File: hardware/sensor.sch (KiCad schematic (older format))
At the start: 4 parts

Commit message: Finished Modulator; still needs Values doe; Fixed Symbol for the HC4046
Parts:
- added C1, C2: C_Small, symbol C_Small
- added R1, R2, R3, R?: R_Small, symbol R_Small
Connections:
- net labels added: +3V3, GND, TX_in, TX_out
- wire segments 0 -> 13
- no-connect marks 0 -> 6
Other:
- moved on the sheet: U?
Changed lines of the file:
@@
 L CD74HC4046 U?
 U 1 1 56DDA4FD
-P 3750 2650
-F 0 "U?" H 3450 3250 60  0000 C CNN
-F 1 "CD74HC4046" H 3700 1850 60  0000 C CNN
-F 2 "Housings_SSOP:TSSOP-16_4.4x5mm_Pitch0.65mm" H 4550 1650 60  0001 C CNN
-F 3 "http://www.ti.com/lit/ds/symlink/cd74hc4046a.pdf" H 4600 1750 60  0001 C CNN
-	1    3750 2650
+P 2700 6150
+F 0 "U?" H 2400 6850 60  0000 C CNN
+F 1 "CD74HC4046" H 2650 5250 60  0000 C CNN
+F 2 "Housings_SSOP:TSSOP-16_4.4x5mm_Pitch0.65mm" H 3500 5150 60  0001 C CNN
+F 3 "http://www.ti.com/lit/ds/symlink/cd74hc4046a.pdf" H 3550 5250 60  0001 C CNN
+	1    2700 6150
 	1    0    0    -1
 $EndComp
@@
 L CD74HC4046 U?
 U 1 1 56DDA564
-P 2300 2700
-F 0 "U?" H 2000 3300 60  0000 C CNN
-F 1 "CD74HC4046" H 2250 1900 60  0000 C CNN
-F 2 "Housings_SSOP:TSSOP-16_4.4x5mm_Pitch0.65mm" H 3100 1700 60  0001 C CNN
-F 3 "http://www.ti.com/lit/ds/symlink/cd74hc4046a.pdf" H 3150 1800 60  0001 C CNN
-	1    2300 2700
+P 2700 3675
+F 0 "U?" H 2400 4375 60  0000 C CNN
+F 1 "CD74HC4046" H 2650 2775 60  0000 C CNN
+F 2 "Housings_SSOP:TSSOP-16_4.4x5mm_Pitch0.65mm" H 3500 2675 60  0001 C CNN
+F 3 "http://www.ti.com/lit/ds/symlink/cd74hc4046a.pdf" H 3550 2775 60  0001 C CNN
+	1    2700 3675
 	1    0    0    -1
 $EndComp
@@
 L SM72485 U?
 U 1 1 56DDC866
-P 9150 2050
-F 0 "U?" H 8950 2350 60  0000 C CNN
-F 1 "SM72485" H 9100 1750 60  0000 C CNN
-F 2 "" H 9000 1800 60  0000 C CNN
-F 3 "" H 9000 1800 60  0000 C CNN
-	1    9150 2050
+P 2475 1500
+F 0 "U?" H 2275 1800 60  0000 C CNN
+F 1 "SM72485" H 2425 1200 60  0000 C CNN
+F 2 "" H 2325 1250 60  0000 C CNN
+F 3 "" H 2325 1250 60  0000 C CNN
+	1    2475 1500
 	1    0    0    -1
 $EndComp
+NoConn ~ 2150 3425
+NoConn ~ 3250 3525
+NoConn ~ 3250 3225
+NoConn ~ 3250 3325
+NoConn ~ 3250 3425
+$Comp
+L GND #PWR?
+U 1 1 56DDF4B2
+P 2150 3525
+F 0 "#PWR?" H 2150 3275 50  0001 C CNN
+F 1 "GND" H 2150 3375 50  0000 C CNN
+F 2 "" H 2150 3525 50  0000 C CNN
+F 3 "" H 2150 3525 50  0000 C CNN
+	1    2150 3525
+	1    0    0    -1
+$EndComp
+Text GLabel 3250 3825 2    60   Output ~ 0
+TX_out
+Wire Wire Line
+	1325 3925 2150 3925
+$Comp
+L GND #PWR?
+U 1 1 56DE0254
+P 1425 4200
+F 0 "#PWR?" H 1425 3950 50  0001 C CNN
+F 1 "GND" H 1425 4050 50  0000 C CNN
+F 2 "" H 1425 4200 50  0000 C CNN
+F 3 "" H 1425 4200 50  0000 C CNN
+	1    1425 4200
+	1    0    0    -1
+$EndComp
+Wire Wire Line
+	1700 3825 2150 3825
+$Comp
+L GND #PWR?
+U 1 1 56DE0651
+P 1750 4425
+F 0 "#PWR?" H 1750 4175 50  0001 C CNN
+F 1 "GND" H 1750 4275 50  0000 C CNN
+F 2 "" H 1750 4425 50  0000 C CNN
+F 3 "" H 1750 4425 50  0000 C CNN
+	1    1750 4425
+	1    0    0    -1
+$EndComp
+$Comp
+L C_Small C1
+U 1 1 56DE088F
+P 3250 4325
+F 0 "C1" H 3260 4395 50  0000 L CNN
+F 1 "C_Small" H 3260 4245 50  0000 L CNN
+F 2 "" H 3250 4325 50  0000 C CNN
+F 3 "" H 3250 4325 50  0000 C CNN
+	1    3250 4325
+	1    0    0    -1
+$EndComp
+NoConn ~ 3250 3975
+Wire Wire Line
+	1850 4075 1750 4075
+Wire Wire Line
+	1750 4075 1750 4425
+Wire Wire Line
+	1850 4275 1750 4275
+Connection ~ 1750 4275
+Wire Wire Line
+	1750 4425 2150 4425
+Text GLabel 1025 3925 0    60   Input ~ 0
+TX_in
+$Comp
+L C_Small C2
+U 1 1 56DE1352
+P 1425 4100
+F 0 "C2" H 1435 4170 50  0000 L CNN
+F 1 "C_Small" H 1435 4020 50  0000 L CNN
+F 2 "" H 1425 4100 50  0000 C CNN
+F 3 "" H 1425 4100 50  0000 C CNN
+	1    1425 4100
+	1    0    0    -1
+$EndComp
+Wire Wire Line
+	1425 4000 1425 3925
+Connection ~ 1425 3925
+$Comp
+L R_Small R3
+U 1 1 56DE1418
+P 1225 3925
+F 0 "R3" V 1300 3850 50  0000 L CNN
+F 1 "R_Small" V 1150 3850 50  0000 L CNN
+F 2 "" H 1225 3925 50  0000 C CNN
+F 3 "" H 1225 3925 50  0000 C CNN
+	1    1225 3925
+	0    1    1    0
+$EndComp
+Wire Wire Line
+	1125 3925 1025 3925
+$Comp
+L R_Small R1
+U 1 1 56DE14BB
+P 1950 4075
+F 0 "R1" V 2025 4000 50  0000 L CNN
+F 1 "R_Small" V 1875 4000 50  0000 L CNN
+F 2 "" H 1950 4075 50  0000 C CNN
+F 3 "" H 1950 4075 50  0000 C CNN
+	1    1950 4075
+	0    1    1    0
+$EndComp
+$Comp
+L R_Small R2
+U 1 1 56DE15BE
+P 1950 4275
+F 0 "R2" V 2025 4200 50  0000 L CNN
+F 1 "R_Small" V 1875 4200 50  0000 L CNN
+F 2 "" H 1950 4275 50  0000 C CNN
+F 3 "" H 1950 4275 50  0000 C CNN
+	1    1950 4275
+	0    1    1    0
+$EndComp
+Wire Wire Line
+	2150 4075 2050 4075
+Wire Wire Line
+	2050 4275 2150 4275
+$Comp
+L R_Small R?
+U 1 1 56DE1837
+P 1700 3425
+F 0 "R?" H 1730 3445 50  0000 L CNN
+F 1 "R_Small" H 1730 3385 50  0000 L CNN
+F 2 "" H 1700 3425 50  0000 C CNN
+F 3 "" H 1700 3425 50  0000 C CNN
+	1    1700 3425
+	1    0    0    -1
+$EndComp
+Wire Wire Line
+	1700 3825 1700 3525
+Wire Wire Line
+	1700 3025 1700 3325
+Wire Wire Line
+	1700 3125 2150 3125
+$Comp
+L +3V3 #PWR?
+U 1 1 56DE1924
+P 1700 3025
+F 0 "#PWR?" H 1700 2875 50  0001 C CNN
+F 1 "+3V3" H 1700 3165 50  0000 C CNN
+F 2 "" H 1700 3025 50  0000 C CNN
+F 3 "" H 1700 3025 50  0000 C CNN
+	1    1700 3025
+	1    0    0    -1
+$EndComp
+Connection ~ 1700 3125
 $EndSCHEMATC

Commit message: Finished Demodulator without fiex values
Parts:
- added C1_RX, C2_RX: C_Small, symbol C_Small
- added JP2_RX, JP3.1, JP3.2, JP3.3, R1_RX, R2_RX, R3_RX: R_Small, symbol R_Small
- added R4_RX: 10k, symbol R_Small
- added R5_RX: 50k, symbol R_Small
- R4_TX: renamed from R?; value R_Small -> 10k
- renumbered C1 to C1_TX, C2 to C2_TX, R1 to R1_TX, R2 to R2_TX, R3 to R3_TX
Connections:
- net labels added: JP2, RX_in, RX_out, VCOin
- wire segments 13 -> 40
- no-connect marks 6 -> 7
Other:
- moved on the sheet: C1_TX, C2_TX, R1_TX, R2_TX, R3_TX, R4_TX, U?

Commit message: Finished LDO for 3V3
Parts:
- added C1_BUCK: 1uF, symbol CP1_Small
- added C2_BUCK: 22uF, symbol CP1_Small
- added C3_BUCK: 0.47uF, symbol CP1_Small
- added C4_BUCK: 10nF, symbol CP1_Small
- added C5_BUCK: 0.1uF, symbol CP1_Small
- added D1_BUCK: D_Schottky_Small, symbol D_Schottky_Small
- added L1_BUCK: 1.2uH, symbol L_Small
- added R3_BUCK: 3k3, symbol R_Small
- added R_CL: 316k, symbol R_Small
- added R_FB1: 5k6, symbol R_Small
- added R_FB2: 1k8, symbol R_Small
- added R_T: 1M8, symbol R_Small
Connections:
- net labels added: SHD, VCC
- wire segments 40 -> 60
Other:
- note added: "Power Supply"
- note added: "Reciever"
- note added: "Transmitter"
- moved on the sheet: U?

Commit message: Started SAM D09 schematic
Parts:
- added D? (x2): Led_Small, symbol Led_Small
- added P?: CONN_01X05, symbol CONN_01X05
- added R?: R_Small, symbol R_Small
- added SW?: Reset, symbol SW_PUSH
- added SW?: Cstm, symbol SW_PUSH
- added X1: UART, symbol CONN_01X04
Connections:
- wire segments 60 -> 67
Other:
- moved on the sheet: U?
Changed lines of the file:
@@
 $Descr A4 11693 8268
 encoding utf-8
-Sheet 1 1
+Sheet 1 3
 Title ""
 Date ""
@@
 L Atmel_SAM_D09 U?
 U 1 1 56DDC7EB
-P 8500 1625
-F 0 "U?" H 8000 2375 60  0000 C CNN
-F 1 "Atmel_SAM_D09" H 8300 475 60  0000 C CNN
-F 2 "Housings_DFN_QFN:QFN-24-1EP_4x4mm_Pitch0.5mm" H 9150 275 60  0001 C CNN
-F 3 "http://www.atmel.com/Images/Atmel-42414-SAM-D09_Datasheet.pdf" H 9550 375 60  0001 C CNN
-	1    8500 1625
+P 8750 2425
+F 0 "U?" H 8250 3175 60  0000 C CNN
+F 1 "Atmel_SAM_D09" H 8550 1275 60  0000 C CNN
+F 2 "Housings_DFN_QFN:QFN-24-1EP_4x4mm_Pitch0.5mm" H 9400 1075 60  0001 C CNN
+F 3 "http://www.atmel.com/Images/Atmel-42414-SAM-D09_Datasheet.pdf" H 9800 1175 60  0001 C CNN
+	1    8750 2425
 	1    0    0    -1
 $EndComp
@@
 Connection ~ 3175 1750
 Wire Wire Line
-	3950 2275 3175 2275
-Wire Wire Line
-	3950 2150 3950 2275
+	3175 2275 3950 2275
+Wire Wire Line
+	3950 2275 3950 2150
 Wire Wire Line
 	3550 2275 3550 2325
@@
 Text Notes 4925 7750 0    60   ~ 0
 Reciever
+$Sheet
+S 7850 5275 1225 625
+U 56E1682E
+F0 "modem_AFE031" 60
+F1 "modem_AFE031.sch" 60
+$EndSheet
+$Sheet
+S 5900 5275 1200 625
+U 56E15A8D
+F0 "modem_TDA5051A" 60
+F1 "modem_TDA5051A.sch" 60
+$EndSheet
+$Comp
+L GND #PWR?
+U 1 1 56E1B7BB
+P 7800 3525
+F 0 "#PWR?" H 7800 3275 50  0001 C CNN
+F 1 "GND" H 7800 3375 50  0000 C CNN
+F 2 "" H 7800 3525 50  0000 C CNN
+F 3 "" H 7800 3525 50  0000 C CNN
+	1    7800 3525
+	1    0    0    -1
+$EndComp
+Wire Wire Line
+	8000 3325 7800 3325
+Wire Wire Line
+	7800 3325 7800 3525
+$Comp
+L +3V3 #PWR?
+U 1 1 56E1B89A
+P 7800 1725
+F 0 "#PWR?" H 7800 1575 50  0001 C CNN
+F 1 "+3V3" H 7800 1865 50  0000 C CNN
+F 2 "" H 7800 1725 50  0000 C CNN
+F 3 "" H 7800 1725 50  0000 C CNN
+	1    7800 1725
+	1    0    0    -1
+$EndComp
+Wire Wire Line
+	8000 1925 7800 1925
+Wire Wire Line
+	7800 1925 7800 1725
+$Comp
+L Led_Small D?
+U 1 1 56E1B95B
+P 10475 2175
+F 0 "D?" H 10425 2300 50  0000 L CNN
+F 1 "Led_Small" H 10300 2075 50  0000 L CNN
+F 2 "" V 10475 2175 50  0000 C CNN
+F 3 "" V 10475 2175 50  0000 C CNN
+	1    10475 2175
+	0    -1   -1   0
+$EndComp
+$Comp
+L Led_Small D?
+U 1 1 56E1BA9C
+P 10125 2200
+F 0 "D?" H 10075 2325 50  0000 L CNN
+F 1 "Led_Small" H 9950 2100 50  0000 L CNN
+F 2 "" V 10125 2200 50  0000 C CNN
+F 3 "" V 10125 2200 50  0000 C CNN
+	1    10125 2200
+	0    -1   -1   0
+$EndComp
+$Comp
+L CONN_01X04 X1
+U 1 1 56E1BAFD
+P 10475 3025
+F 0 "X1" H 10475 3275 50  0000 C CNN
+F 1 "UART" V 10575 3025 50  0000 C CNN
+F 2 "" H 10475 3025 50  0000 C CNN
+F 3 "" H 10475 3025 50  0000 C CNN
+	1    10475 3025
+	1    0    0    -1
+$EndComp
+$Comp
+L SW_PUSH SW?
+U 1 1 56E1C074
+P 7025 2025
+F 0 "SW?" H 7175 2135 50  0000 C CNN
+F 1 "Reset" H 7025 1945 50  0000 C CNN
+F 2 "" H 7025 2025 50  0000 C CNN
+F 3 "" H 7025 2025 50  0000 C CNN
+	1    7025 2025
+	1    0    0    -1
+$EndComp
+$Comp
+L SW_PUSH SW?
+U 1 1 56E1C541
+P 10250 3950
+F 0 "SW?" H 10400 4060 50  0000 C CNN
+F 1 "Cstm" H 10250 3870 50  0000 C CNN
+F 2 "" H 10250 3950 50  0000 C CNN
+F 3 "" H 10250 3950 50  0000 C CNN
+	1    10250 3950
+	1    0    0    -1
+$EndComp
+$Comp
+L CONN_01X05 P?
+U 1 1 56E1D11A
+P 6750 2850
+F 0 "P?" H 6750 3150 50  0000 C CNN
+F 1 "CONN_01X05" V 6850 2850 50  0000 C CNN
+F 2 "" H 6750 2850 50  0000 C CNN
+F 3 "" H 6750 2850 50  0000 C CNN
+	1    6750 2850
+	1    0    0    -1
+$EndComp
+$Comp
+L GND #PWR?
+U 1 1 56E1D419
+P 6725 2025
+F 0 "#PWR?" H 6725 1775 50  0001 C CNN
+F 1 "GND" H 6725 1875 50  0000 C CNN
+F 2 "" H 6725 2025 50  0000 C CNN
+F 3 "" H 6725 2025 50  0000 C CNN
+	1    6725 2025
+	1    0    0    -1
+$EndComp
+$Comp
+L R_Small R?
+U 1 1 56E1D47B
+P 7450 1825
+F 0 "R?" H 7480 1845 50  0000 L CNN
+F 1 "R_Small" H 7480 1785 50  0000 L CNN
+F 2 "" H 7450 1825 50  0000 C CNN
+F 3 "" H 7450 1825 50  0000 C CNN
+	1    7450 1825
+	1    0    0    -1
+$EndComp
+Wire Wire Line
+	7800 1725 7450 1725
+Wire Wire Line
+	7450 1925 7450 2025
+Wire Wire Line
+	7325 2025 8000 2025
+Connection ~ 7450 2025
 $EndSCHEMATC

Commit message: Started redoing buck; added LMR16006 component
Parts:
- removed U?: SM72485, symbol SM72485
- added R2, R3: 100, symbol R_Small
- added R4: 10k, symbol R_Small
- added U?: LMR16006, TO_SOT_Packages_SMD:TSOT-6-MK06A, symbol LMR16006
- C1_BUCK1: renamed from C1_BUCK; footprint (none) -> Capacitors_SMD:C_0805; symbol CP1_Small -> C_Small
- C1_RX1: renamed from C1_RX; footprint (none) -> Capacitors_SMD:C_0603
- C1_TX1: renamed from C1_TX; footprint (none) -> Capacitors_SMD:C_0603
- C2_BUCK1: renamed from C2_BUCK; footprint (none) -> Capacitors_SMD:C_0603; symbol CP1_Small -> C_Small
- C2_RX1: renamed from C2_RX; footprint (none) -> Capacitors_SMD:C_0603
- C2_TX1: renamed from C2_TX; footprint (none) -> Capacitors_SMD:C_0603
- C3_BUCK1: renamed from C3_BUCK; footprint (none) -> Capacitors_SMD:C_0603; symbol CP1_Small -> C_Small
- C4_BUCK1: renamed from C4_BUCK; footprint (none) -> Capacitors_SMD:C_0603; symbol CP1_Small -> C_Small
- C5_BUCK1: renamed from C5_BUCK; footprint (none) -> Capacitors_SMD:C_0805; symbol CP1_Small -> C_Small
- D_BLUE1: renamed from D?; value Led_Small -> BLUE; footprint (none) -> Resistors_SMD:R_0603
- D_RED1: renamed from D?; value Led_Small -> RED; footprint (none) -> Resistors_SMD:R_0603
- JP2_RX1: renamed from JP2_RX; footprint (none) -> Resistors_SMD:R_0603
- JP3.1, JP3.2, JP3.3: footprint (none) -> Resistors_SMD:R_0603
- R1: renamed from R?; footprint (none) -> LEDs:LED_0603
- R1_RX1: renamed from R1_RX; footprint (none) -> LEDs:LED_0603
- gave numbers to parts that had none: 6
- renumbered D1_BUCK to D1_BUCK1, L1_BUCK to L1_BUCK1, R1_TX to R1_TX1, R2_RX to R2_RX1, R2_TX to R2_TX1, R3_BUCK to R3_BUCK1, R3_RX to R3_RX1, R3_TX to R3_TX1, R4_RX to R4_RX1, R4_TX to R4_TX1, R5_RX to R5_RX1, R_CL to R_CL1, R_T to R_T1
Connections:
- net labels added: BLUE_ON, RED_ON
- wire segments 67 -> 81
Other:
- note added: "MCU"
- note added: "SW_CSTM"
- moved on the sheet: D1_BUCK1, D_BLUE1, D_RED1, L1_BUCK1, P1, R1, R3_BUCK1, R_CL1, R_FB1, R_FB2, R_T1, SW1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

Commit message: New buck schema is done
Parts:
- removed C1_BUCK1: 1uF, Capacitors_SMD:C_0805, symbol C_Small
- removed C3_BUCK1: 0.47uF, Capacitors_SMD:C_0603, symbol C_Small
- removed D1_BUCK1: D_Schottky_Small, symbol D_Schottky_Small
- removed R3_BUCK1: 3k3, symbol R_Small
- removed R_CL1: 316k, symbol R_Small
- added D?: D_Schottky_Small, symbol D_Schottky_Small
- C_BOOT: renamed from C4_BUCK1; value 10nF -> 100nF
- C_in: renamed from C5_BUCK1; value 0.1uF -> 2.2uF
- C_out: renamed from C2_BUCK1; value 22uF -> 10uF
- L1_BUCK: renamed from L1_BUCK1; value 1.2uH -> 22uH
- R_FB1: renamed from R_FB2; value 1k8 -> 33k
- R_FB2: renamed from R_FB1; value 5k6 -> 10k
- gave numbers to parts that had none: 1
- renumbered R_T1 to R?
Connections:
- wire segments 81 -> 73
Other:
- moved on the sheet: C_BOOT, C_in, C_out, L1_BUCK, R?, R_FB1, R_FB2

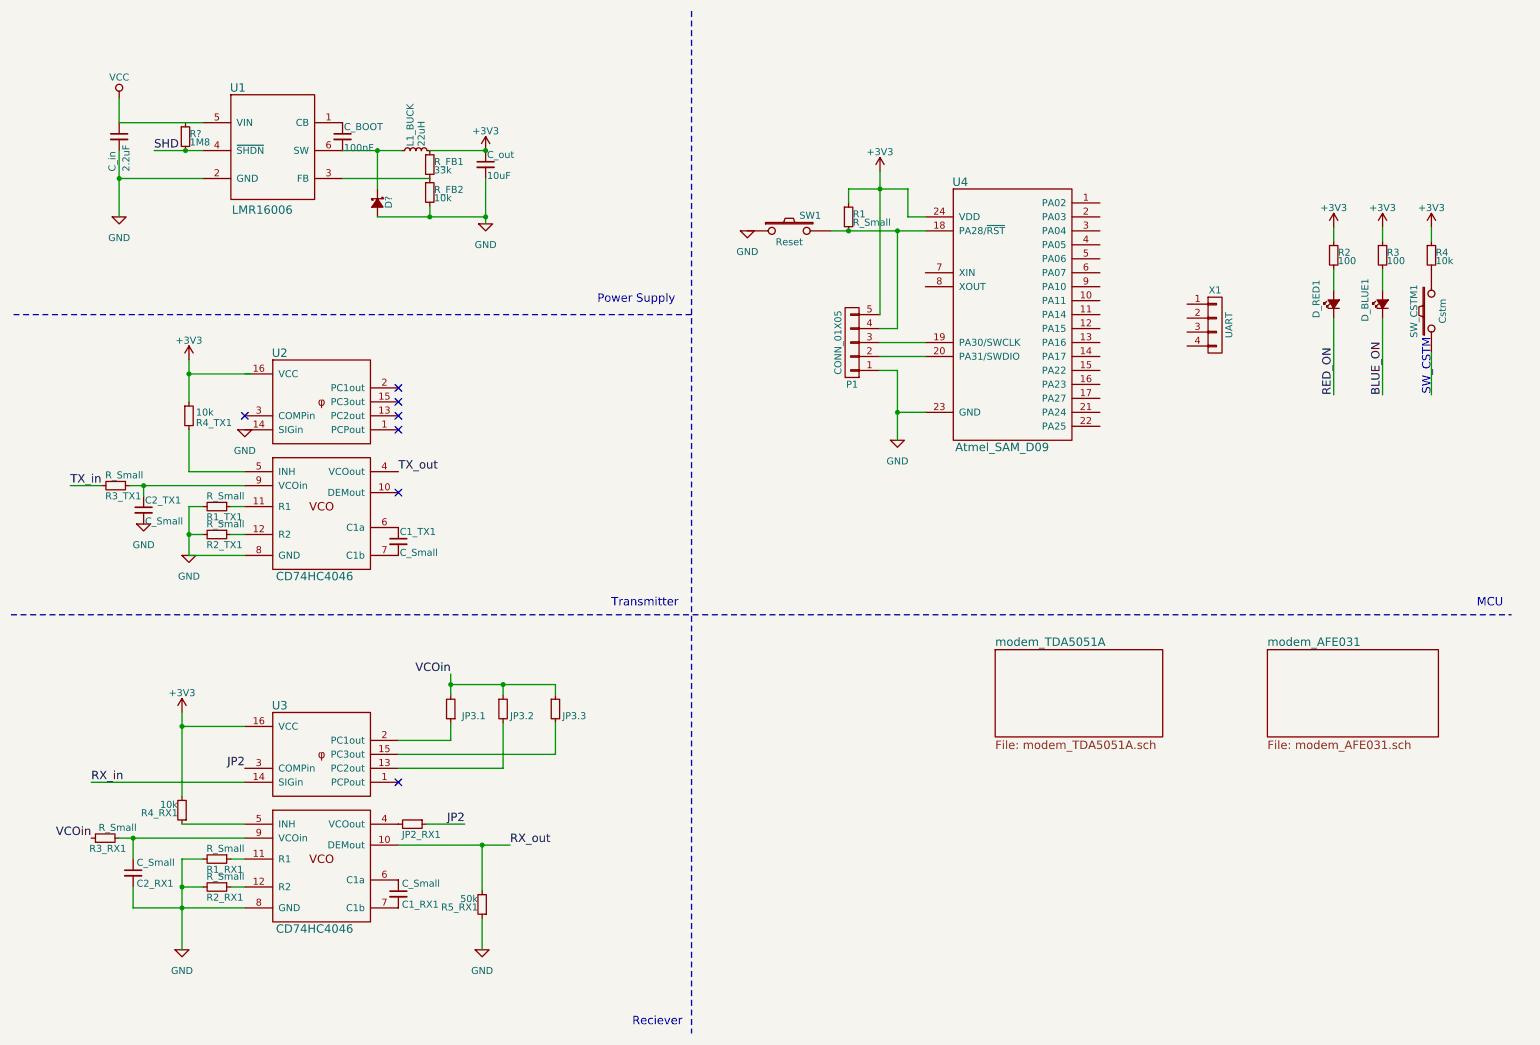
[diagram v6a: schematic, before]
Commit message: Added trimmer to adjust the frequency range; Needs amp and SAMD09
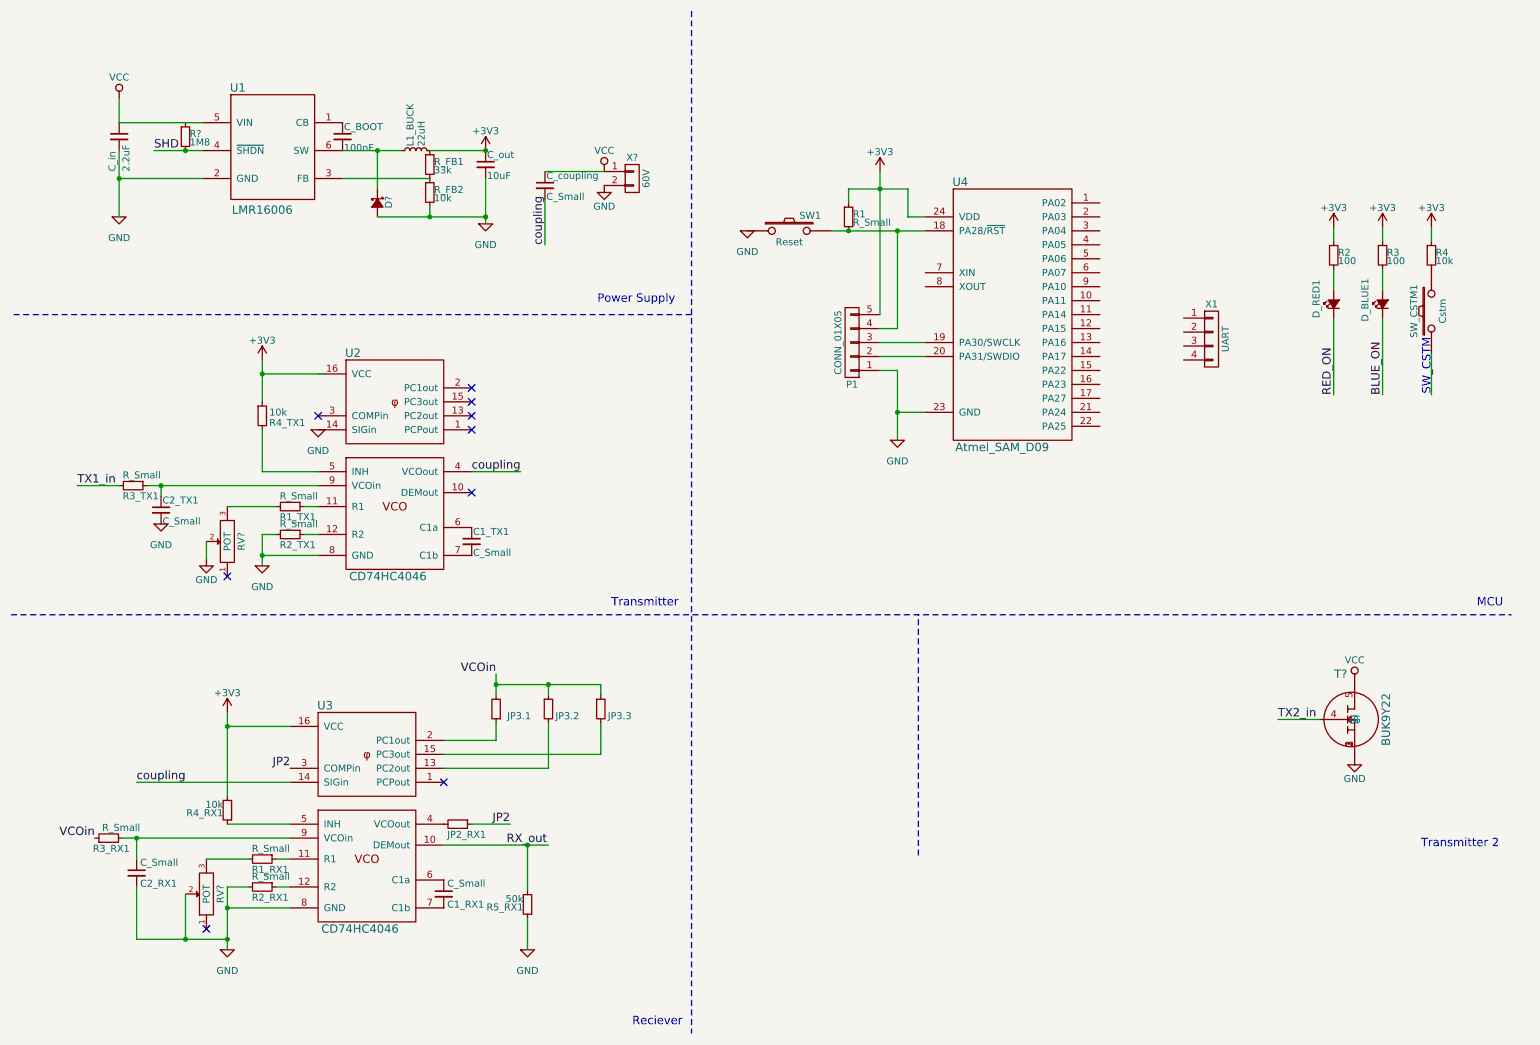
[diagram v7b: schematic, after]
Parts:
- added C_coupling: C_Small, symbol C_Small
- added RV? (x2): POT, pro4:EVM-1USX30B14, symbol POT
- added T?: BUK9Y22, TO_SOT_Packages_SMD:SOT-669_LFPAK_ThermalVias-1, symbol BUK9Y22
- added X?: 60V, symbol CONN_01X02
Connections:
- net labels added: TX1_in, TX2_in, coupling
- net labels removed: RX_in, TX_in, TX_out
- wire segments 73 -> 101
- no-connect marks 7 -> 9
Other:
- note added: "Transmitter 2"
- moved on the sheet: C1_RX1, C1_TX1, C2_RX1, C2_TX1, JP2_RX1, JP3.1, JP3.2, JP3.3, R1_RX1, R1_TX1, R2_RX1, R2_TX1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

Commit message: Finished schema for prototype; Started placing of the parts; BUCK and TX done
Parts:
- added C1, C2, C5: C_Small, Capacitors_SMD:C_0603, symbol C_Small
- added C3: 0.1u, Capacitors_SMD:C_0603, symbol C_Small
- added C4: 1u, Capacitors_SMD:C_0603, symbol C_Small
- added R10, R11: R_Small, Resistors_SMD:R_0603, symbol R_Small
- added R6: 600k, Resistors_SMD:R_0805, symbol R_Small
- added R7: 33k, Resistors_SMD:R_0603, symbol R_Small
- added R8, R9: 100k, Resistors_SMD:R_0603, symbol R_Small
- added U5: OPA376AIDCK, TO_SOT_Packages_SMD:SC-70-6, symbol OPA376AIDCK
- C_coupling1: renamed from C_coupling; footprint (none) -> Capacitors_SMD:C_0805
- D1: renamed from D?; footprint (none) -> Diodes_SMD:SOD-123
- L1_BUCK1: renamed from L1_BUCK; footprint (none) -> SMD_Packages:SMD-1210_Pol
- P1: footprint (none) -> Pin_Headers:Pin_Header_Angled_1x05
- R1_TX1, R2, R2_RX1, R2_TX1, R3, R3_RX1, R3_TX1, R4, R4_RX1, R4_TX1, R5_RX1, R_FB1, R_FB2: footprint (none) -> Resistors_SMD:R_0603
- R5: renamed from R?; footprint (none) -> Resistors_SMD:R_0805
- SW1, SW_CSTM1: footprint (none) -> Buttons_Switches_SMD:SW_SPST_PTS645
- X1: footprint (none) -> Connectors_Molex:Connector_Molex_PicoBlade_53261-0471
- X2: renamed from X?; footprint (none) -> Pin_Headers:Pin_Header_Angled_1x02
- gave numbers to parts that had none: 3
- renumbered C_BOOT to C_BOOT1, C_in to C_in1, C_out to C_out1
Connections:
- net labels added: RX2_out, RX_in, SW_CSTM, adc_0
- net labels removed: RX_out, TX2_in
- wire segments 101 -> 104
- no-connect marks 9 -> 20
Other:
- note added: "Interface"
- note added: "Sensor"
- note removed: "SW_CSTM"
- moved on the sheet: C1_RX1, C2_RX1, JP2_RX1, JP3.1, JP3.2, JP3.3, R1_RX1, R2_RX1, R3_RX1, R4_RX1, R5_RX1, RV1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
